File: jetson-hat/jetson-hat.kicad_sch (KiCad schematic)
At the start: 1 part, among them J1 GPIO

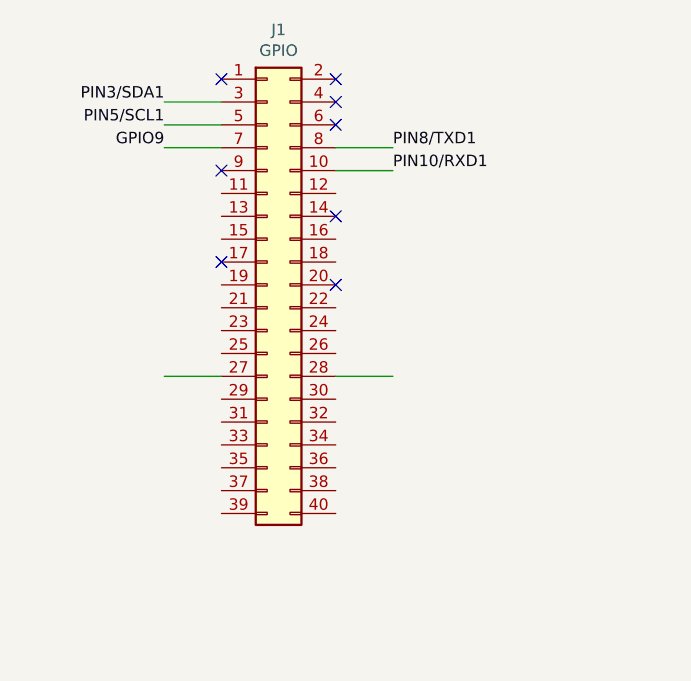
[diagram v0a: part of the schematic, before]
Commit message: Add Jetson 40 Pin connector pins
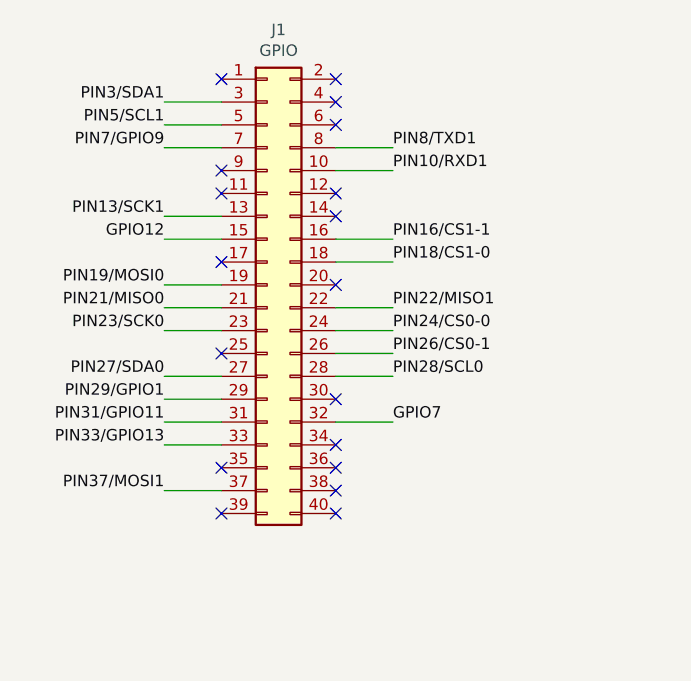
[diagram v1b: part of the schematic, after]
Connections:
- net PIN13/SCK1: now reaches J1.13 (Pin_13)
- net GPIO12: now reaches J1.15 (Pin_15)
- net PIN16/CS1-1: now reaches J1.16 (Pin_16)
- net PIN18/CS1-0: now reaches J1.18 (Pin_18)
- net PIN19/MOSI0: now reaches J1.19 (Pin_19)
- net PIN21/MISO0: now reaches J1.21 (Pin_21)
- net PIN22/MISO1: now reaches J1.22 (Pin_22)
- net PIN23/SCK0: now reaches J1.23 (Pin_23)
- net PIN24/CS0-0: now reaches J1.24 (Pin_24)
- net PIN26/CS0-1: now reaches J1.26 (Pin_26)
- net PIN27/SDA0: now reaches J1.27 (Pin_27)
- net PIN28/SCL0: now reaches J1.28 (Pin_28)
- net PIN29/GPIO1: now reaches J1.29 (Pin_29)
- net PIN31/GPIO11: now reaches J1.31 (Pin_31)
- net GPIO7: now reaches J1.32 (Pin_32)
- net PIN33/GPIO13: now reaches J1.33 (Pin_33)
- net PIN37/MOSI1: now reaches J1.37 (Pin_37)
- net GPIO9 renamed PIN7/GPIO9
- no-connect marks 8 -> 18

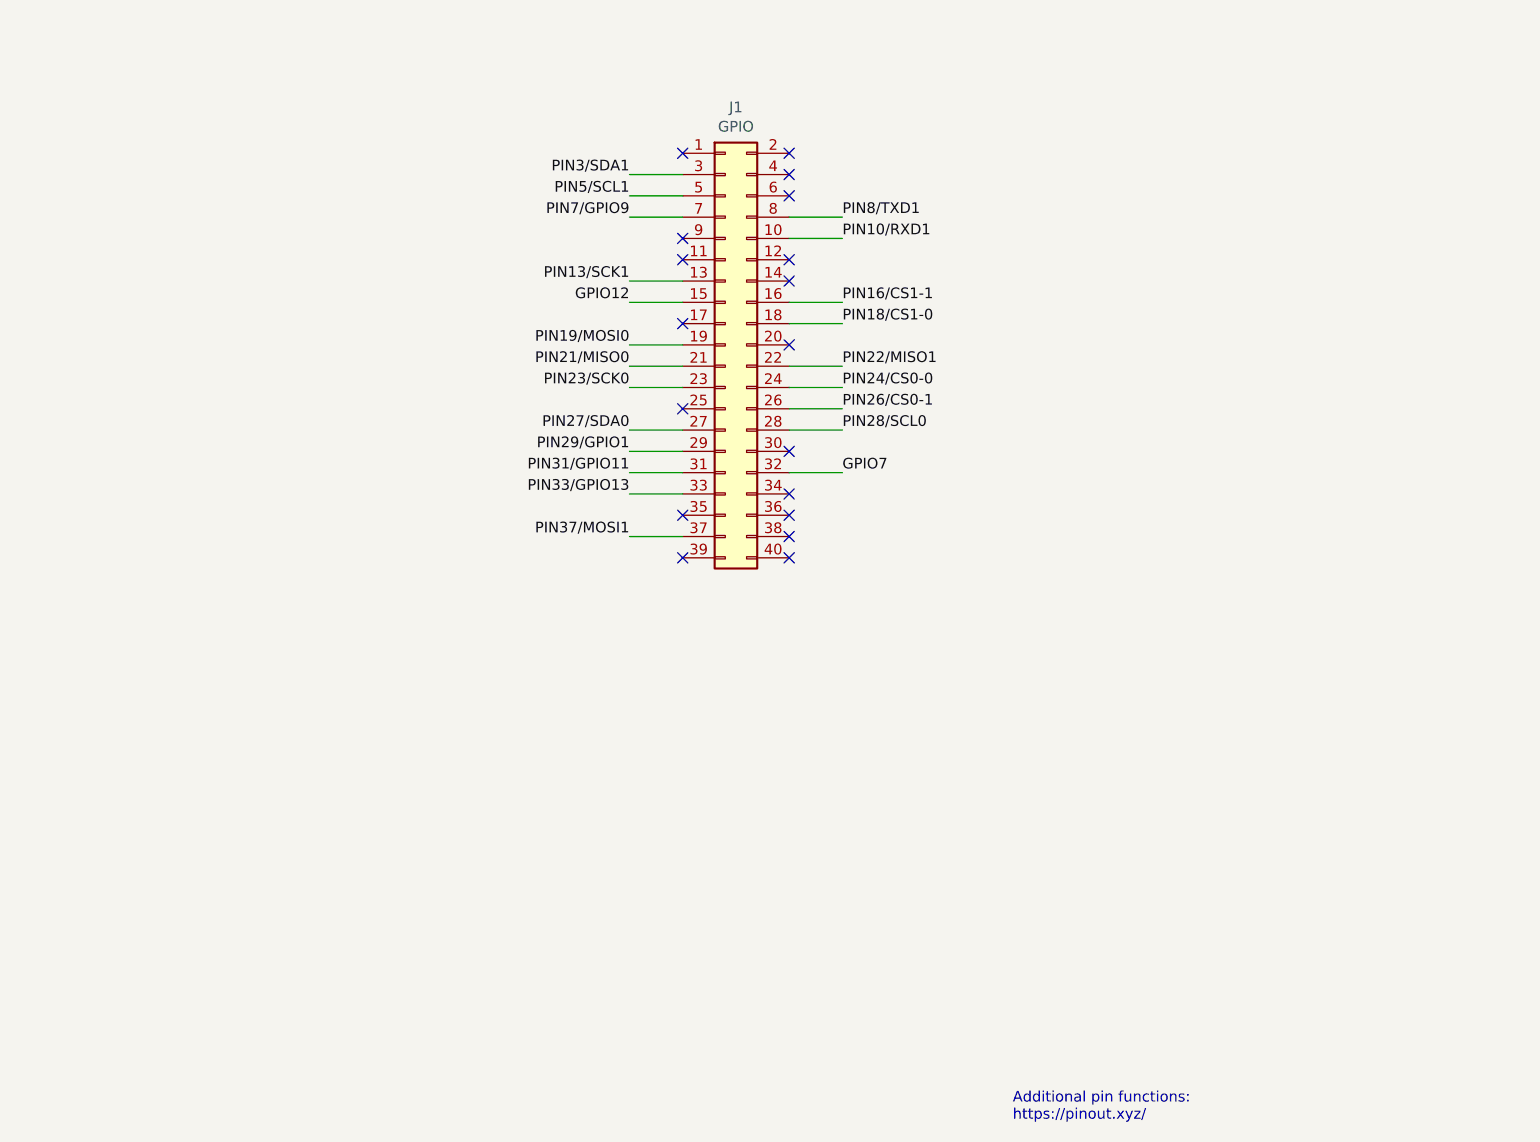
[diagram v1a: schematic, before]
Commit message: Add SC16IS752IPW Symbol and some Notes
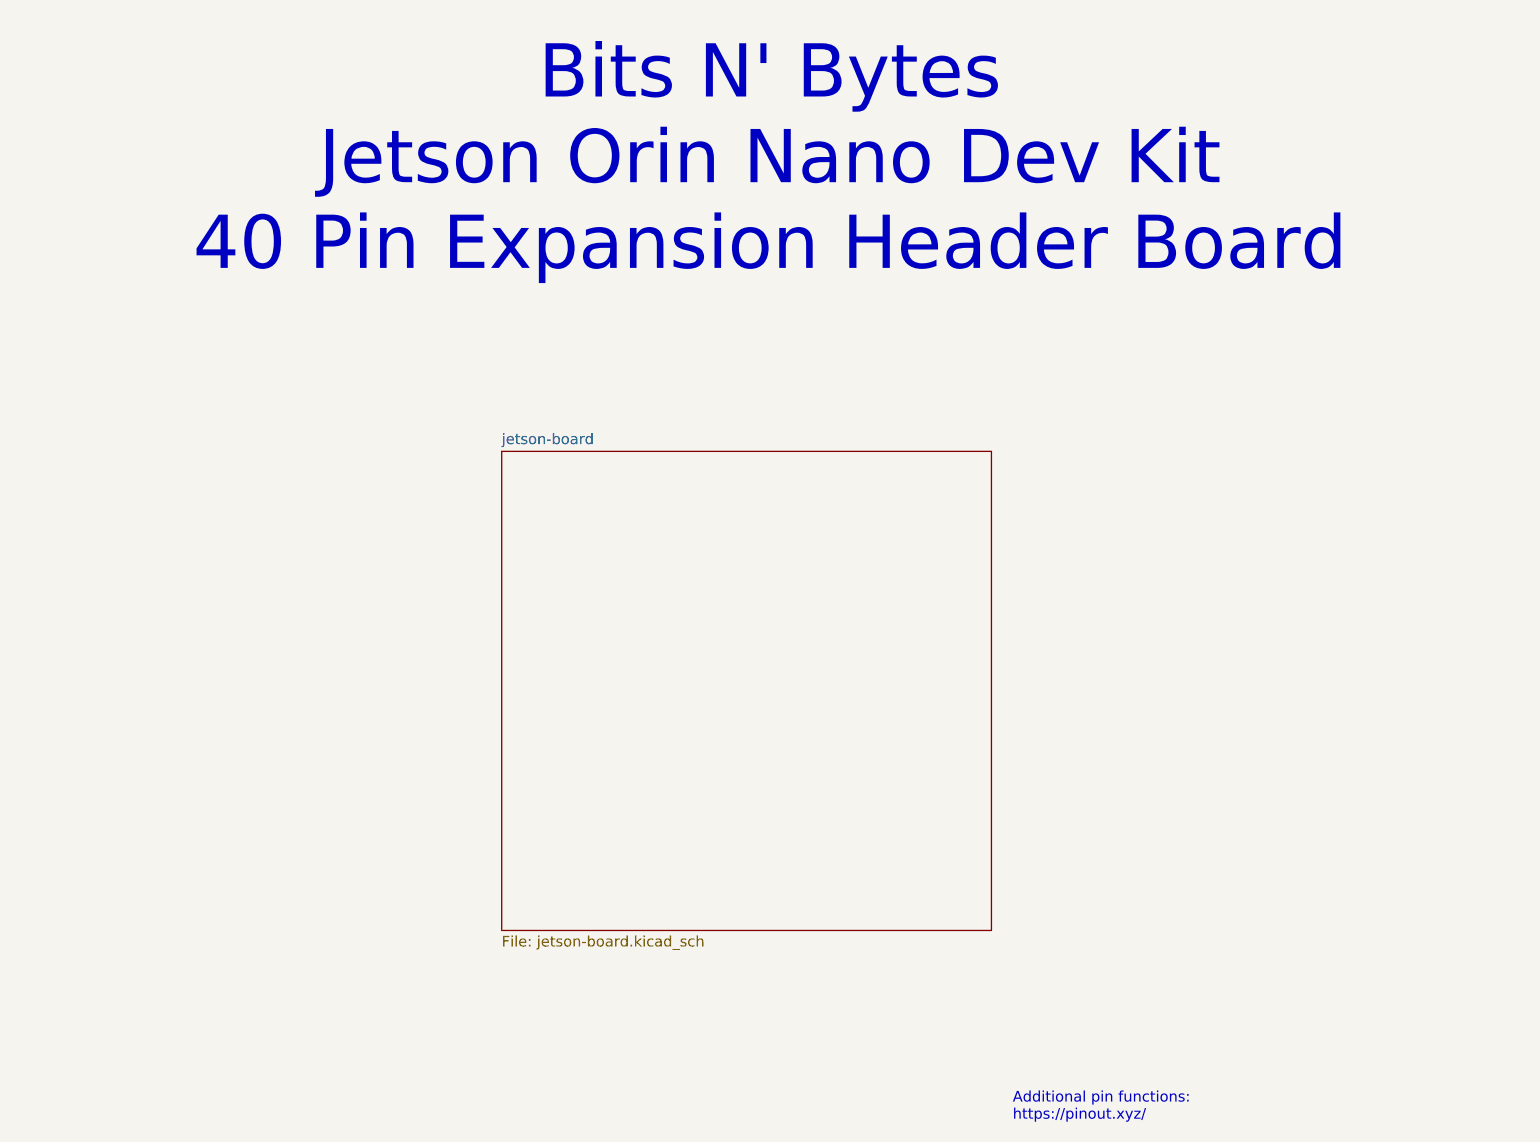
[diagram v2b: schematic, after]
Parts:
- removed J1: GPIO, Connector_PinSocket_2.54mm:PinSocket_2x20_P2.54mm_Vertical, symbol Connector_Generic:Conn_02x20_Odd_Even
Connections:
- no-connect marks 18 -> 0
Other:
- added sheet jetson-board (jetson-board.kicad_sch)
- note added: "Bits N' Bytes Jetson Orin Nano Dev Kit 40 Pin Expansion Header Board"
